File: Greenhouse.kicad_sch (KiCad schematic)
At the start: 26 parts, among them J1 Conn_01x03, J2 Conn_02x20_Odd_Even, U2 IS31FL3197, U3 LTV-847S

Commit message: updated schematic & pcb with latest part selections
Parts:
- removed C5, C6, C7, C8: C, Greenhouse-Footprints:CAPC3216X180N, symbol Device:C
- removed R1, R2, R3, R4: R_US, Resistor_SMD:R_1206_3216Metric, symbol Device:R_US
- removed U2: IS31FL3197, Greenhouse-Footprints:QFN-16_EP_4x4_Pitch0.65mm, symbol Greenhouse-Symbols:IS31FL3197-QFLS2-TR
- added RN1: CAY16-271J4LF, Greenhouse-Footprints:RESCAF80P320X160X60-8N, symbol Greenhouse-Symbols:EXB-38V271JV
- C1: value C -> 1µF
- C2: value C_Polarized -> 330µF; footprint Greenhouse-Footprints:CAP_EEEFT1H331AP -> Greenhouse-Footprints:CAPPM7343X310N
- C3, C4: value C -> .1µF
- RPIZ1: renamed from J2; footprint Greenhouse-Footprints:Raspi Zero W Socket SMD -> Greenhouse-Footprints:Raspi Zero W Socket TH
- U1: renamed from U3; footprint LTV-847S:SOIC254P1016X460-16N -> Greenhouse-Footprints:DIP880W50P254L2034H450Q16
- renumbered F2 to F1, F3 to F2, F1 to FUSE1, L4 to L1, L3 to L2, L2 to L3, L1 to L4, U1 to TRANSFORMER1
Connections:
- net +3V3: now also U1.1, U1.3, U1.5, U1.7
- net GND: now also TRANSFORMER1.5 (-V); no longer TRANSFORMER1.8 (-V)
- net GPIO13: now also F1.2 (Pin_2)
- net GPIO14: now also F2.2 (Pin_2)
- net GPIO21: now also RN1.3
- net GPIO22: now also RN1.2
- net GPIO23: now also RN1.1
- net GPIO30: now also RN1.4
- net LINE: now also J1.2 (Pin_2); no longer J1.3 (Pin_3)
- net NEUT: now also J1.3 (Pin_3); no longer J1.2 (Pin_2)
- net PWM0: no longer F2.2 (Pin_2)
- net PWM1: no longer F1.2 (Pin_2)
- net at U1.8: now also RN1.5
- net at U1.6: now also RN1.6
- net at U1.4: now also RN1.7
- net at U1.2: now also RN1.8
- net at U1.10: now also L4.2 (Pin_2); no longer L1.2 (Pin_2)
- net at U1.11: now also L3.1 (Pin_1); no longer L2.1 (Pin_1)
- net at U1.12: now also L3.2 (Pin_2); no longer L2.2 (Pin_2)
- net at U1.13: now also L2.1 (Pin_1); no longer L3.1 (Pin_1)
- net at U1.14: now also L2.2 (Pin_2); no longer L3.2 (Pin_2)
- net at U1.15: now also L1.1 (Pin_1); no longer L4.1 (Pin_1)
- net at U1.16: now also L1.2 (Pin_2); no longer L4.2 (Pin_2)
- net at U1.9: now also L4.1 (Pin_1); no longer L1.1 (Pin_1)
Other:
- note added: "Lights"
- note removed: "The Alt Light"
- moved on the sheet: L1, L2, L3, L4, U1

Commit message: Finalized PCB layout, updated/added footprint models
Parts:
- removed L1, L2, L3, L4: Conn_01x02_Socket, Greenhouse-Footprints:TE_282834-2, symbol Connector:Conn_01x02_Socket
- added J2: 282834-8, Greenhouse-Footprints:TE_282834-8, symbol Greenhouse-Symbols:282834-8
- C2: footprint Greenhouse-Footprints:CAPPM7343X310N -> Greenhouse-Footprints:CAP_EEEFT1H331AP
- F1, F2: footprint Greenhouse-Footprints:TE_282834-3 -> Greenhouse-Footprints:Fan Header 3,4-pin through hole right angle; symbol Connector_Generic:Conn_01x03 -> Connector_Generic:Conn_01x04
- renumbered C4 to C5
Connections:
- net GND: now also F1.4 (Pin_4), F2.4 (Pin_4); no longer F1.1 (Pin_1), F2.1 (Pin_1)
- net GPIO13: no longer F1.2 (Pin_2)
- net GPIO14: no longer F2.2 (Pin_2)
- net GPIO2: now also F1.2 (Pin_2)
- net GPIO3: now also F2.2 (Pin_2)
- net PWM0: now also F2.1 (Pin_1)
- net PWM1: now also F1.1 (Pin_1)
- net at U1.10: now also J2.2
- net at U1.11: now also J2.3
- net at U1.12: now also J2.4
- net at U1.13: now also J2.5
- net at U1.14: now also J2.6
- net at U1.15: now also J2.7
- net at U1.16: now also J2.8
- net at U1.9: now also J2.1
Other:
- moved on the sheet: I2C1

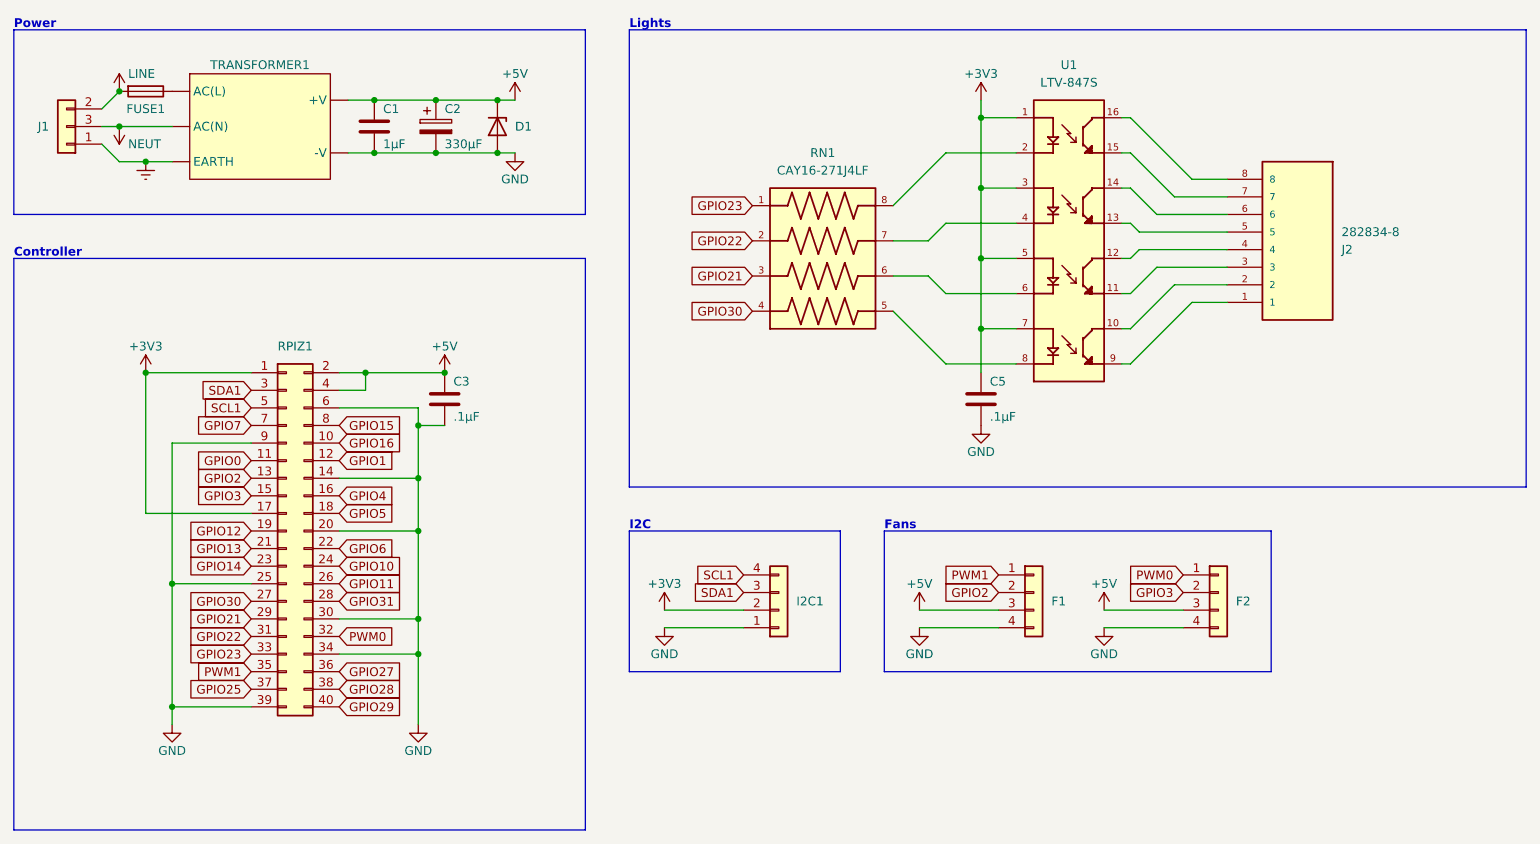
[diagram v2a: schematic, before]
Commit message: Added customized footprints for the three edge headers to include guide marks, fixed bug with GPIO net labels
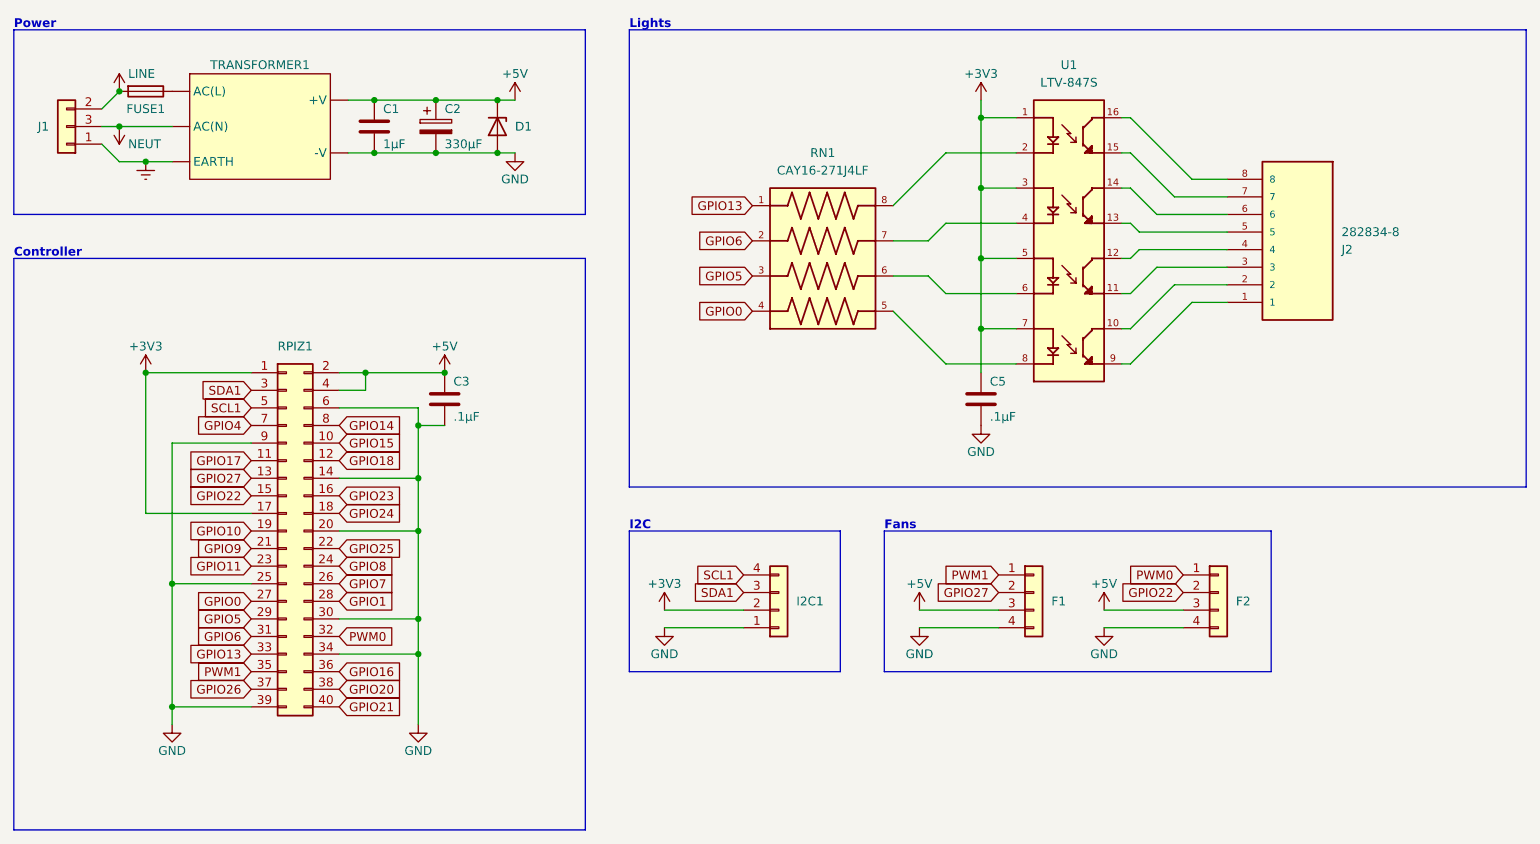
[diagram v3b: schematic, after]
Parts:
- F1, F2: footprint Greenhouse-Footprints:Fan Header 3,4-pin through hole right angle -> Greenhouse-Footprints:Fan Header 3,4-pin through hole right angle, custom
- I2C1: footprint Greenhouse-Footprints:JST_S4B-PH-SM4-TB -> Greenhouse-Footprints:JST_S4B-PH-SM4-TB, custom
- J2: footprint Greenhouse-Footprints:TE_282834-8 -> Greenhouse-Footprints:TE_282834-8, custom
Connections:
- net GPIO12 is gone; now on net GPIO10: RPIZ1.19 (Pin_19)
- net GPIO2 is gone; now on net GPIO27: F1.2 (Pin_2), RPIZ1.13 (Pin_13)
- net GPIO29 is gone; now on net GPIO21: RPIZ1.40 (Pin_40)
- net GPIO3 is gone; now on net GPIO22: F2.2 (Pin_2), RPIZ1.15 (Pin_15)
- net GPIO30 is gone; now on net GPIO0: RN1.4, RPIZ1.27 (Pin_27)
- net GPIO31 is gone; now on net GPIO1: RPIZ1.28 (Pin_28)
- net GPIO0: no longer RPIZ1.11 (Pin_11)
- net GPIO1: no longer RPIZ1.12 (Pin_12)
- net GPIO10: no longer RPIZ1.24 (Pin_24)
- net GPIO11: now also RPIZ1.23 (Pin_23); no longer RPIZ1.26 (Pin_26)
- net GPIO13: now also RN1.1, RPIZ1.33 (Pin_33); no longer RPIZ1.21 (Pin_21)
- net GPIO14: now also RPIZ1.8 (Pin_8); no longer RPIZ1.23 (Pin_23)
- net GPIO15: now also RPIZ1.10 (Pin_10); no longer RPIZ1.8 (Pin_8)
- net GPIO16: now also RPIZ1.36 (Pin_36); no longer RPIZ1.10 (Pin_10)
- net GPIO21: no longer RN1.3, RPIZ1.29 (Pin_29)
- net GPIO22: no longer RN1.2, RPIZ1.31 (Pin_31)
- net GPIO23: now also RPIZ1.16 (Pin_16); no longer RN1.1, RPIZ1.33 (Pin_33)
- net GPIO25: now also RPIZ1.22 (Pin_22); no longer RPIZ1.37 (Pin_37)
- net GPIO27: no longer RPIZ1.36 (Pin_36)
- net GPIO4: now also RPIZ1.7 (Pin_7); no longer RPIZ1.16 (Pin_16)
- net GPIO5: now also RN1.3, RPIZ1.29 (Pin_29); no longer RPIZ1.18 (Pin_18)
- net GPIO6: now also RN1.2, RPIZ1.31 (Pin_31); no longer RPIZ1.22 (Pin_22)
- net GPIO7: now also RPIZ1.26 (Pin_26); no longer RPIZ1.7 (Pin_7)
- net GPIO28 renamed GPIO20
- new net GPIO17: RPIZ1.11 (Pin_11)
- new net GPIO18: RPIZ1.12 (Pin_12)
- new net GPIO24: RPIZ1.18 (Pin_18)
- new net GPIO26: RPIZ1.37 (Pin_37)
- new net GPIO8: RPIZ1.24 (Pin_24)
- new net GPIO9: RPIZ1.21 (Pin_21)
